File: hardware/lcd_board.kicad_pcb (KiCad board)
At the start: 2 copper layers, 80 x 50 mm, 127 parts, among them J1 HDMI-A receptacle, J2 USB-C (power + touch USB), J3 AT070TN92 FPC (0.5mm 50P, top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, J4 Touch FPC 6P 0.5mm, J5 SWD/UART, J6 Touch alt. JST-SH 6P, Q1 AO3401A, Q2 2N7002, SW1 BOOT (DFU), U1 LT8619C, U10 STM32F072CBT6, U2 AMS1117-3.3, U3 AMS1117-1.8, U4 USBLC6-2SC6, U7 TPS61040, U8 LM321, U9 TPS61165, Y1 25MHz 12pF

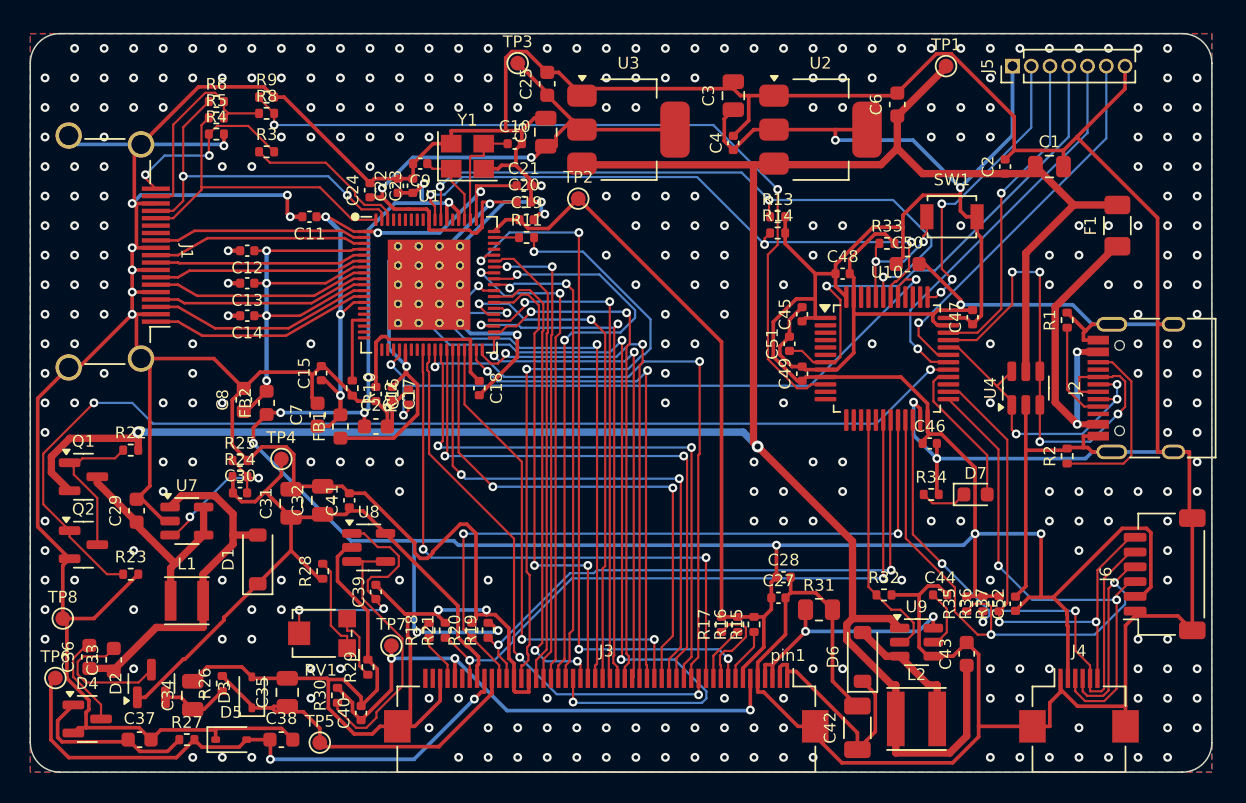
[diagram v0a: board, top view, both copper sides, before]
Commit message: Use 0603 passives and remove the alternative touch connector J6
- All 0402 resistors/capacitors are now 0603 (LCSC numbers updated to the
  matching 0603 basic parts); bulk/high-voltage caps stay 0805/1206
- J6 (JST-SH touch header) removed
- LT8619C decoupling pre-routes, crystal and REXT placement adapted to the
  larger footprints; RGB bus escape area under the chip kept free
- Re-routed (Freerouting 2.0.1), DRC: 0 errors, 0 unconnected
- Schematic, BOM/CPL, gerbers, images and README regenerated

Co-Authored-By: Claude Opus 5.5 <noreply@anthropic.com>
Claude-Session: https://claude.ai/code/session_01X8BrieHZtCS6HfoR48ML9y
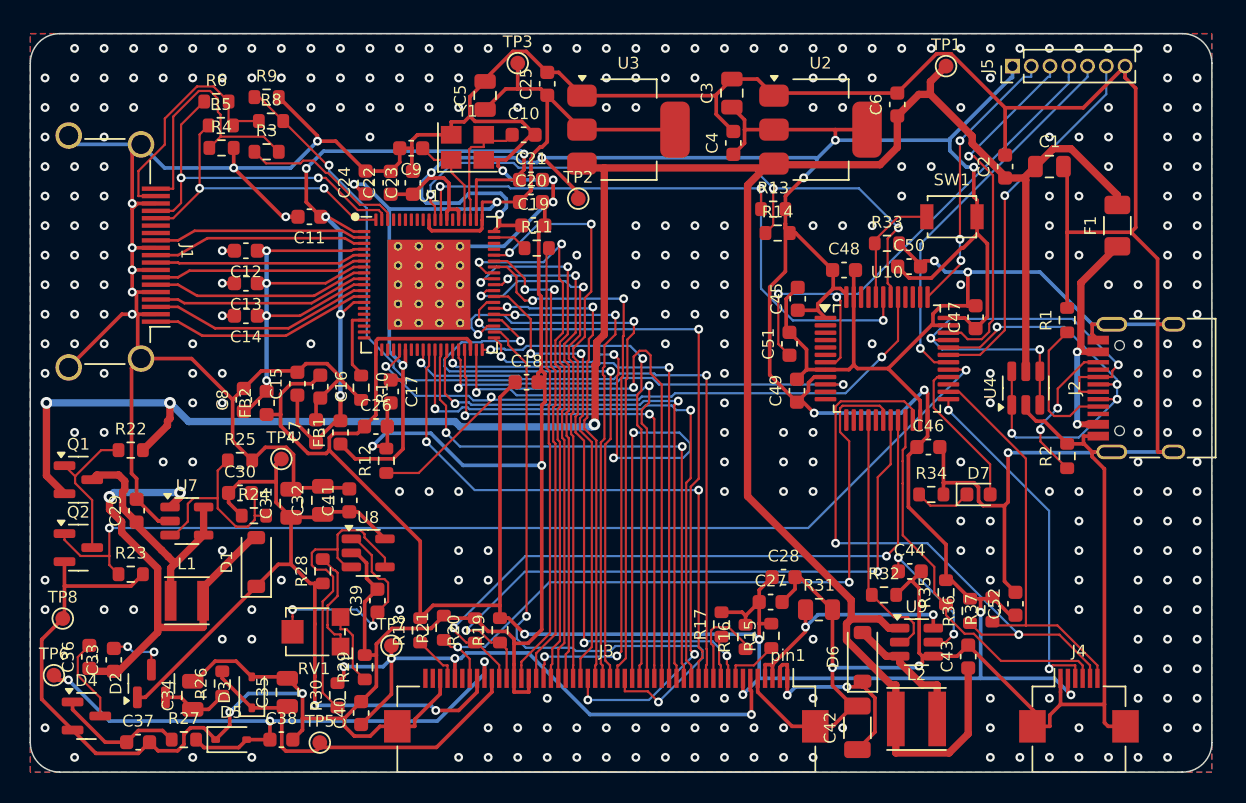
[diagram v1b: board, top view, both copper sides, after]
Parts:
- removed J6: Touch alt. JST-SH 6P, Connector_JST:JST_SH_SM06B-SRSS-TB_1x06-1MP_P1.00mm_Horizontal
- C10, C11, C12, C13, C14, C15, C16, C17, C18, C19, C2, C20, C21, C22, C23, C24, C27, C28, C30, C39, C4, C40, C41, C44, C45, C46, C47, C48, C49, C51, C52, C9: footprint Capacitor_SMD:C_0402_1005Metric -> Capacitor_SMD:C_0603_1608Metric
- R1, R10, R11, R12, R13, R14, R15, R16, R17, R18, R19, R2, R20, R21, R22, R23, R24, R25, R26, R27, R28, R29, R3, R30, R32, R33, R34, R35, R36, R37, R4, R5, R6, R8, R9: footprint Resistor_SMD:R_0402_1005Metric -> Resistor_SMD:R_0603_1608Metric
- moved C5 4.80 mm to (130.8, 84.2)
- moved R12 4.57 mm to (124.1, 108.9)
- moved C16 3.80 mm to (119.6, 103.9)
- moved C18 3.22 mm to (133.6, 103.6), turned to 0 degrees
- moved R24 2.80 mm to (115.1, 112.6)
- moved C44 2.60 mm to (159.5, 116.4)
- moved C15 1.77 mm to (118.1, 103.7)
- moved R35 1.60 mm to (162.0, 117.8)
- moved R15 1.40 mm to (150.2, 120.8)
- moved C9 1.21 mm to (125.8, 87.8)
- moved C49 1.20 mm to (151.9, 104.2)
- moved C7 1.13 mm to (119.3, 106.9)
- moved C45 1.09 mm to (152.0, 98.0)
- moved R36 1.00 mm to (163.6, 119.1)
- moved R4 1.00 mm to (112.9, 87.7)
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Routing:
- net LCD_R5: track 59.4 -> 35.7 mm, vias 4 -> 2
- net GND: track 616.0 -> 595.2 mm, vias 328 -> 318
- net TP_SCL: track 45.2 -> 26.0 mm, vias 2 -> 0
- net LCD_R7: track 32.5 -> 49.5 mm, vias 2 -> 4
- net +5V: track 168.9 -> 185.3 mm, vias 2 -> 3
- net +1V8A: track 37.5 -> 52.1 mm
- net +3V3: track 305.2 -> 291.0 mm
- net LCD_DCLK: track 43.1 -> 30.2 mm, vias 2 -> 0
- net LCD_G5: track 33.3 -> 43.4 mm, vias 2 -> 4
- net TP_INT: track 33.9 -> 23.8 mm
- net AVDD: track 48.7 -> 58.1 mm, vias 0 -> 2
- net LCD_R1: track 32.1 -> 41.2 mm, vias 2 -> 4
- net USB_DM: track 20.9 -> 30.0 mm, vias 3 -> 4
- net AVDD_SW: track 24.3 -> 33.3 mm, vias 0 -> 2
- net LCD_G4: track 34.7 -> 43.6 mm
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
